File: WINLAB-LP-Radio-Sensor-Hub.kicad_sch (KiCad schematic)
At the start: 0 parts

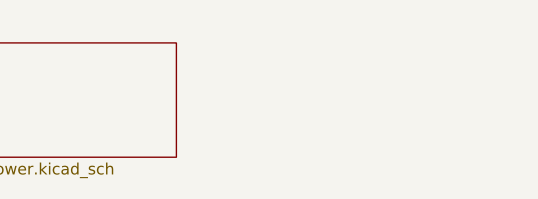
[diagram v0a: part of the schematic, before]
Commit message: add backscatter and active radio components
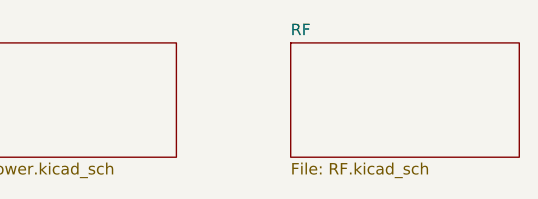
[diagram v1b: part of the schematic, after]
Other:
- added sheet RF (RF.kicad_sch)
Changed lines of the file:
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@@
 	(paper "A4")
+	(sheet
+		(at 114.3 38.1)
+		(size 25.4 12.7)
+		(exclude_from_sim no)
+		(in_bom yes)
+		(on_board yes)
+		(dnp no)
+		(fields_autoplaced yes)
+		(stroke
+			(width 0.1524)
+			(type solid)
+		)
+		(fill
+			(color 0 0 0 0)
+		)
+		(property "Sheetname" "RF"
+			(at 114.3 37.3884 0)
+			(show_name no)
+			(do_not_autoplace no)
+			(effects
+				(font
+					(size 1.27 1.27)
+				)
+				(justify left bottom)
+			)
+		)
+		(property "Sheetfile" "RF.kicad_sch"
+			(at 114.3 51.3846 0)
+			(show_name no)
+			(do_not_autoplace no)
+			(effects
+				(font
+					(size 1.27 1.27)
+				)
+				(justify left top)
+			)
+		)
+		(instances
+			(project "WINLAB-LP-Radio-Sensor-Hub"
+				(path "/0de7ee4a-bb98-4bc6-bb89-3afafc4b94b5"
+					(page "4")
+				)
+			)
+		)
+	)
 	(sheet
 		(at 76.2 38.1)

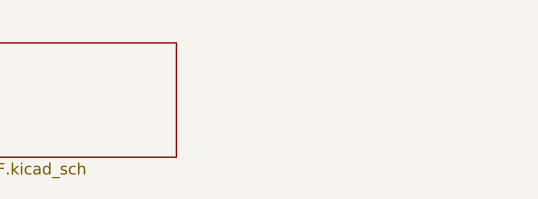
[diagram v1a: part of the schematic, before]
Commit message: add IO ports, begin layout
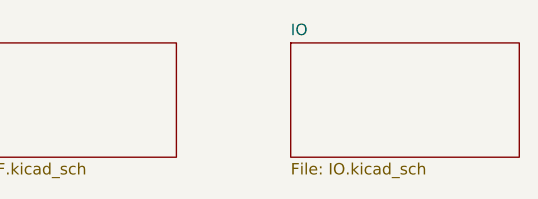
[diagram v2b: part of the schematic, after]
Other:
- added sheet IO (IO.kicad_sch)
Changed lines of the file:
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@@
+	)
+	(sheet
+		(at 152.4 38.1)
+		(size 25.4 12.7)
+		(exclude_from_sim no)
+		(in_bom yes)
+		(on_board yes)
+		(dnp no)
+		(fields_autoplaced yes)
+		(stroke
+			(width 0.1524)
+			(type solid)
+		)
+		(fill
+			(color 0 0 0 0)
+		)
+		(property "Sheetname" "IO"
+			(at 152.4 37.3884 0)
+			(show_name no)
+			(do_not_autoplace no)
+			(effects
+				(font
+					(size 1.27 1.27)
+				)
+				(justify left bottom)
+			)
+		)
+		(property "Sheetfile" "IO.kicad_sch"
+			(at 152.4 51.3846 0)
+			(show_name no)
+			(do_not_autoplace no)
+			(effects
+				(font
+					(size 1.27 1.27)
+				)
+				(justify left top)
+			)
+		)
+		(instances
+			(project "WINLAB-LP-Radio-Sensor-Hub"
+				(path "/0de7ee4a-bb98-4bc6-bb89-3afafc4b94b5"
+					(page "5")
+				)
+			)
+		)
 	)
 	(sheet
